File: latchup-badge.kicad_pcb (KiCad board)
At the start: 2 copper layers, 85.7 x 54 mm, 47 parts, among them J1 USB_C_Receptacle_USB2.0, J2 Connector_Generic:Conn_02x06_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, J3 Connector_Generic:Conn_02x06_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, J4 Connector_Generic:Conn_02x05_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, SW1 SW_Push, SW2 SW_Push, U1 ICE40UP5K-SG48ITR, U2 TLV70012_SOT23-5, U3 TLV70033_SOT23-5, U4 M25PX32-VMW, U5 LY68L6400, X1 ASE-12.000MHz

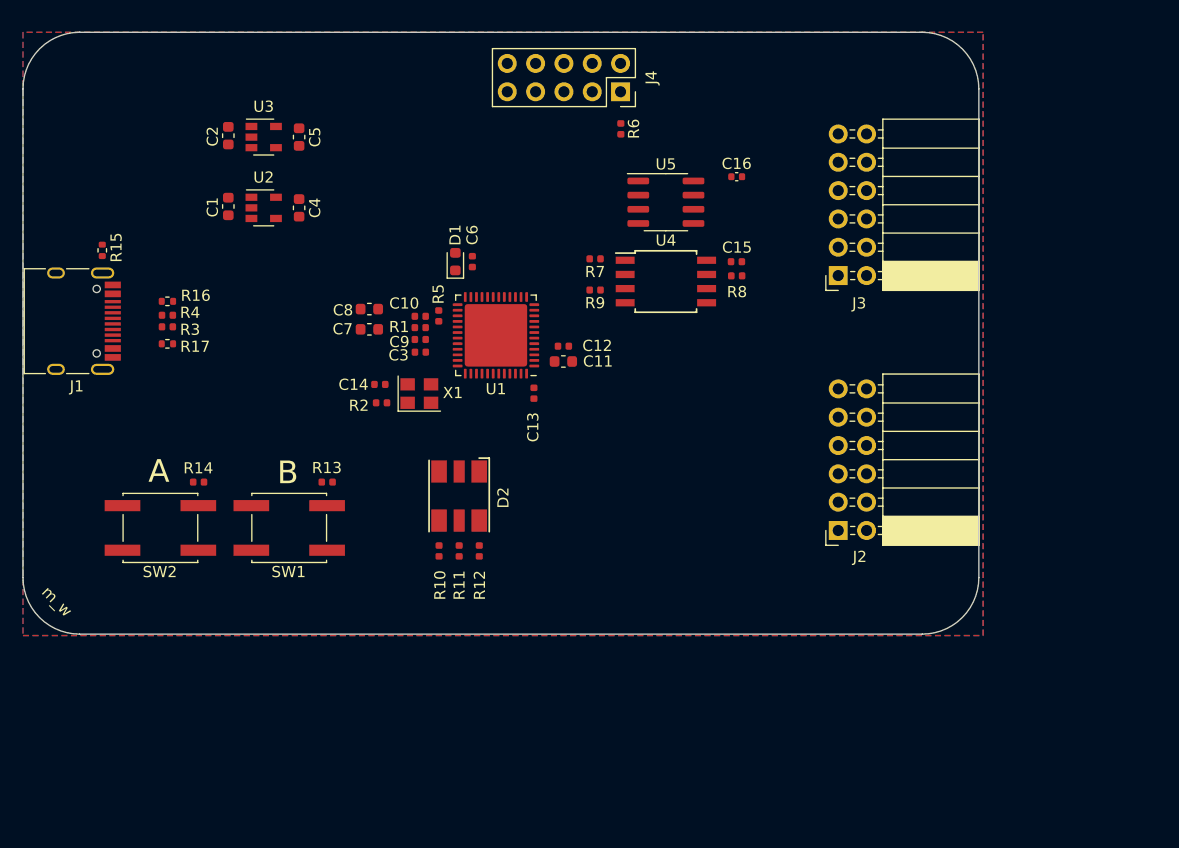
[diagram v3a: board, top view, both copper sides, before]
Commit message: Use the PMOD pinout from icebreaker bitsy breakout
Signed-off-by: Michael Welling <mwelling@ieee.org>
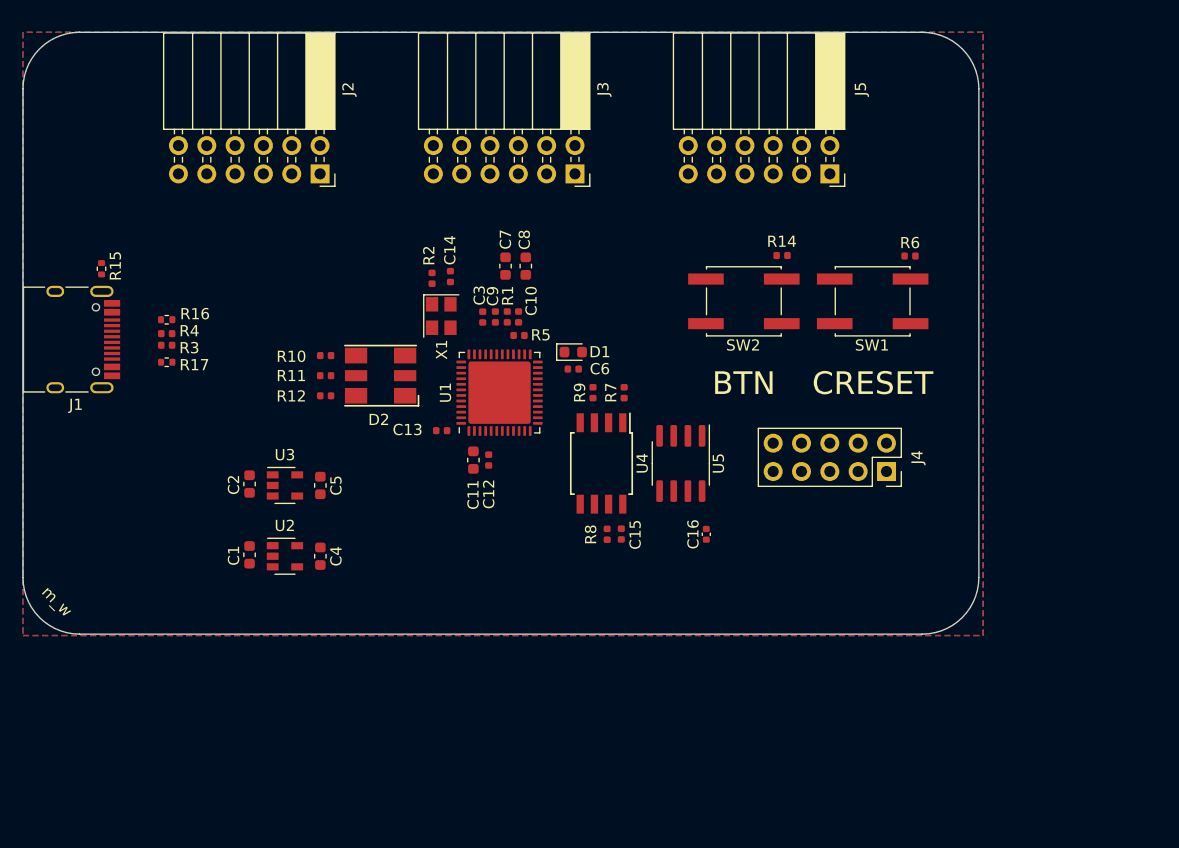
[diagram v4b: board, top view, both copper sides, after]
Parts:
- removed R13: 10K, Resistor_SMD:R_0402_1005Metric
- added J5: Connector_Generic:Conn_02x06_Odd_Even, Connector_PinSocket_2.54mm:PinSocket_2x06_P2.54mm_Horizontal, F.Cu at (148.6, 63.5)
- moved J2 56.4 mm to (102.8, 63.5), turned to -90 degrees
- moved SW1 56.1 mm to (152.4, 74.9)
- moved R14 56.1 mm to (144.3, 70.8)
- moved SW2 56.1 mm to (140.8, 74.9)
- moved J4 41.6 mm to (153.6, 90.2)
- moved C16 32.2 mm to (137.5, 95.8), turned to 90 degrees
- moved C2 31.3 mm to (96.5, 91.3)
- moved C4 31.3 mm to (102.9, 97.8)
- moved U2 31.3 mm to (99.7, 97.8)
- moved C5 31.3 mm to (102.9, 91.4)
- moved U3 31.3 mm to (99.7, 91.4)
- moved C1 31.3 mm to (96.5, 97.7)
- moved R6 28.3 mm to (155.8, 70.9), turned to 0 degrees
- moved C15 26.5 mm to (129.9, 95.8), turned to 90 degrees
- moved R8 25.9 mm to (128.6, 95.8), turned to -90 degrees
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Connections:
- net Net-(U1-Pad35) renamed /PIN35
- J2 pad 1: /J2_P1 -> +3V3
- J2 pad 10: +3V3 -> /PIN45
- J2 pad 11: GND -> /PIN47
- J2 pad 12: GND -> /PIN44
- J2 pad 2: /J2_P2 -> +3V3
- J2 pad 3: /J2_P3 -> GND
- J2 pad 4: /J2_P4 -> GND
- J2 pad 5: /J2_P5 -> /PIN9
- J2 pad 6: /J2_P6 -> /PIN10
- J2 pad 7: /J2_P7 -> /PIN4
- J2 pad 8: /J2_P8 -> /PIN3
- J2 pad 9: +3V3 -> /PIN48
- J3 pad 1: /J3_P1 -> +3V3
- J3 pad 10: +3V3 -> /PIN31
- J3 pad 11: GND -> /PIN43
- J3 pad 12: GND -> /PIN36
- J3 pad 2: /J3_P2 -> +3V3
- J3 pad 3: /J3_P3 -> GND
- J3 pad 4: /J3_P4 -> GND
- J3 pad 5: /J3_P5 -> /PIN28
- J3 pad 6: /J3_P6 -> /PIN34
- J3 pad 7: /J3_P7 -> /PIN26
- J3 pad 8: /J3_P8 -> /PIN27
- J3 pad 9: +3V3 -> /PIN32
- R3 pad 1: /USBD- -> /USBD_N
- R4 pad 1: /USBD+ -> /USBD_P
- R5 pad 1: Net-(R5-Pad1) -> /USB_DET
- R5 pad 2: /USBD+ -> /USBD_P
- SW1 pad 2: /BTN_B -> /CRESET
- U1 pad 10: /J3_P6 -> /PIN10
- U1 pad 11: /J3_P5 -> /PIN11
- U1 pad 12: /J3_P8 -> /PIN12
- U1 pad 13: /J3_P7 -> /PIN13
- U1 pad 18: /RX -> /FLASH_IO2_WP
- U1 pad 19: /TX -> /FLASH_IO3_HLD
- U1 pad 2: unconnected-(U1-Pad2) -> /BTN_A
- U1 pad 20: /FLASH_IO3_HLD -> /PIN20
- U1 pad 21: /FLASH_IO2_WP -> /PIN21
- U1 pad 23: /BTN_B -> /PIN23
- U1 pad 25: /BTN_A -> /PIN25
- U1 pad 26: /USBD- -> /PIN26
- U1 pad 27: /USBD+ -> /PIN27
- U1 pad 28: Net-(R5-Pad1) -> /PIN28
- U1 pad 3: /SS_PSRAM -> /PIN3
- U1 pad 31: unconnected-(U1-Pad31) -> /PIN31
- U1 pad 32: unconnected-(U1-Pad32) -> /PIN32
- U1 pad 34: unconnected-(U1-Pad34) -> /PIN34
- U1 pad 36: /J2_P2 -> /PIN36
- U1 pad 37: /J2_P1 -> /USB_DET
- U1 pad 38: /J2_P4 -> /USBD_N
- U1 pad 4: unconnected-(U1-Pad4) -> /PIN4
- U1 pad 42: /J2_P3 -> /USBD_P
- U1 pad 43: /J2_P6 -> /PIN43
- U1 pad 44: /J2_P5 -> /PIN44
- U1 pad 45: /J2_P8 -> /PIN45
- U1 pad 46: /J2_P7 -> /PIN46
- U1 pad 47: /J3_P2 -> /PIN47
- U1 pad 48: /J3_P1 -> /PIN48
- U1 pad 6: /J3_P4 -> /SS_PSRAM
- U1 pad 9: /J3_P3 -> /PIN9
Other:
- board text added: "BTN"
- board text added: "CRESET"
- board text removed: "A"
- board text removed: "B"

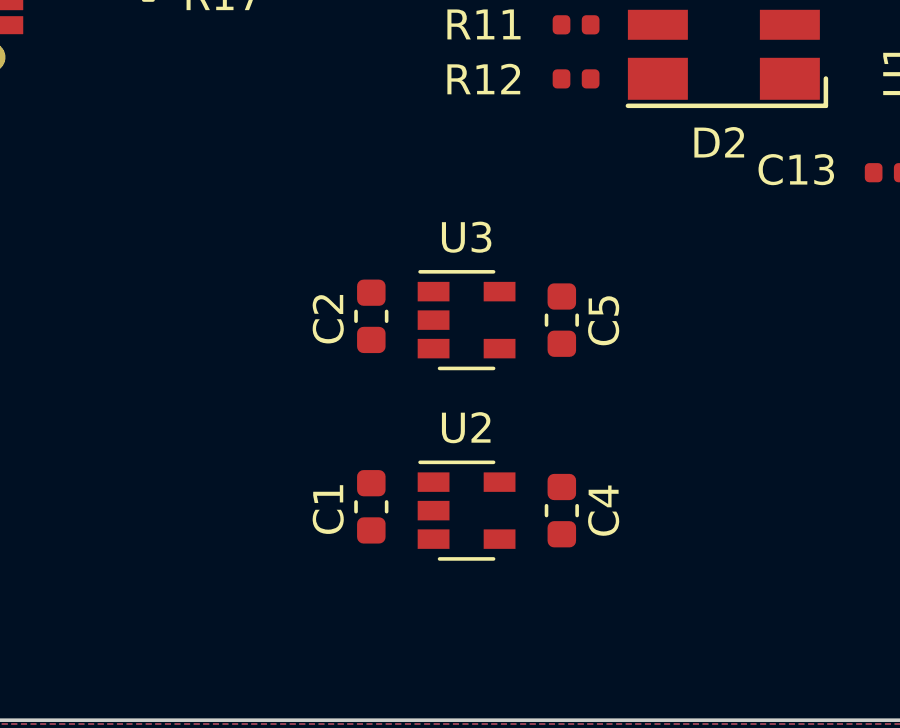
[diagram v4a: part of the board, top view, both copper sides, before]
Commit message: Add delay to 3.3V enable
The 1.2V rail should be up before 3.3V.

Signed-off-by: Michael Welling <mwelling@ieee.org>
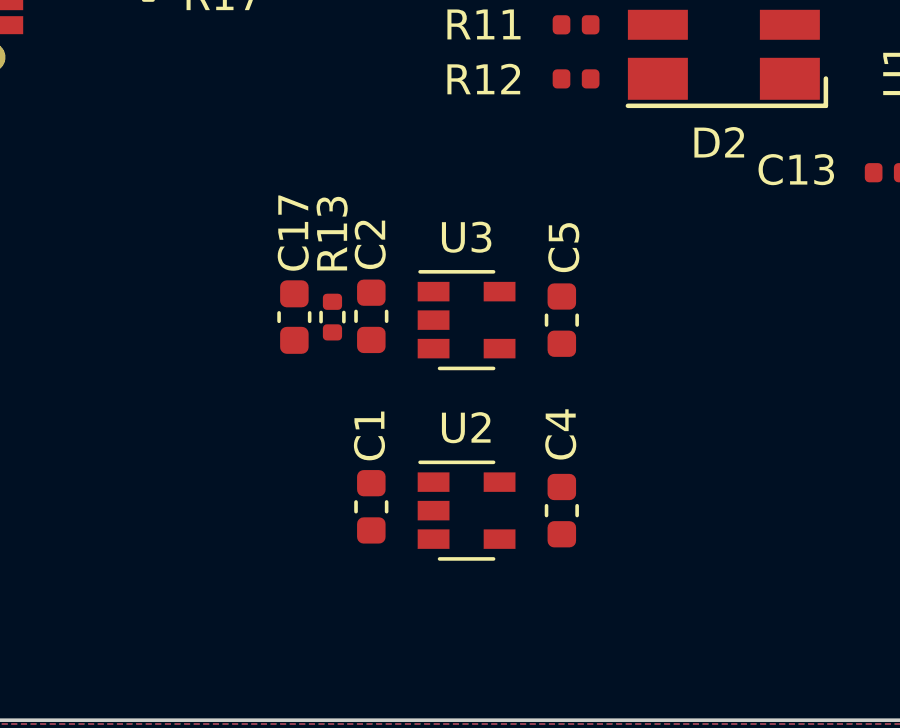
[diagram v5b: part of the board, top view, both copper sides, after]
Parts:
- added C17: 1uF, Capacitor_SMD:C_0603_1608Metric, F.Cu at (94.0, 91.3)
- added R13: 10K, Resistor_SMD:R_0402_1005Metric, F.Cu at (95.2, 91.3)
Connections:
- J4 pad 4: /TX -> unconnected-(J4-Pad4)
- J4 pad 6: /RX -> unconnected-(J4-Pad6)
- U3 pad 3: +5V -> Net-(U3-Pad3)
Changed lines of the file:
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@@
   (net 41 "/PIN25")
   (net 42 "/USBD_N")
-  (net 43 "/RX")
-  (net 44 "/TX")
+  (net 43 "Net-(U3-Pad3)")
+  (net 44 "unconnected-(J4-Pad4)")
   (net 45 "/CDONE")
   (net 46 "/CRESET")
@@
   (net 61 "/USB_DET")
   (net 62 "/PIN35")
+  (net 63 "unconnected-(J4-Pad6)")
   (footprint "Capacitor_SMD:C_0603_1608Metric" (layer "F.Cu")
     (at 96.52 97.663 -90)
@@
     (property "Sheetname" "")
     (attr smd)
-    (fp_text reference "C1" (at 0.066288 1.399799 90) (layer "F.SilkS")
+    (fp_text reference "C1" (at -2.3876 0.0254 90) (layer "F.SilkS")
       (effects (font (size 1 1) (thickness 0.15)))
     )
@@
     (property "Sheetname" "")
     (attr smd)
-    (fp_text reference "C5" (at 0 -1.43 90) (layer "F.SilkS")
+    (fp_text reference "C5" (at -2.4384 -0.1016 90) (layer "F.SilkS")
       (effects (font (size 1 1) (thickness 0.15)))
     )
@@
       (net 8 "GND") (pinfunction "GND") (pintype "power_in"))
     (pad "3" smd rect locked (at -1.1 0.95) (size 1.06 0.65) (layers "F.Cu" "F.Paste" "F.Mask")
-      (net 9 "+5V") (pinfunction "EN") (pintype "input"))
+      (net 43 "Net-(U3-Pad3)") (pinfunction "EN") (pintype "input"))
     (pad "4" smd rect locked (at 1.1 0.95) (size 1.06 0.65) (layers "F.Cu" "F.Paste" "F.Mask")
       (net 22 "unconnected-(U3-Pad4)") (pinfunction "NC") (pintype "no_connect"))
@@
     (property "Sheetname" "")
     (attr smd)
-    (fp_text reference "C4" (at 0 -1.43 90) (layer "F.SilkS")
+    (fp_text reference "C4" (at -2.54 0 90) (layer "F.SilkS")
       (effects (font (size 1 1) (thickness 0.15)))
     )
@@
     (property "Sheetname" "")
     (attr smd)
-    (fp_text reference "C2" (at 0.066288 1.399799 90) (layer "F.SilkS")
+    (fp_text reference "C2" (at -2.413 0 90) (layer "F.SilkS")
       (effects (font (size 1 1) (thickness 0.15)))
     )
@@
       (net 20 "/ICE40_SPI_SO") (pinfunction "Pin_3") (pintype "passive"))
     (pad "4" thru_hole oval locked (at -2.54 2.54 270) (size 1.7 1.7) (drill 1) (layers *.Cu *.Mask)
-      (net 44 "/TX") (pinfunction "Pin_4") (pintype "passive"))
+      (net 44 "unconnected-(J4-Pad4)") (pinfunction "Pin_4") (pintype "passive"))
     (pad "5" thru_hole oval locked (at 0 5.08 270) (size 1.7 1.7) (drill 1) (layers *.Cu *.Mask)
       (net 19 "/ICE40_SPI_SCK") (pinfunction "Pin_5") (pintype "passive"))
     (pad "6" thru_hole oval locked (at -2.54 5.08 270) (size 1.7 1.7) (drill 1) (layers *.Cu *.Mask)
-      (net 43 "/RX") (pinfunction "Pin_6") (pintype "passive"))
+      (net 63 "unconnected-(J4-Pad6)") (pinfunction "Pin_6") (pintype "passive"))
     (pad "7" thru_hole oval locked (at 0 7.62 270) (size 1.7 1.7) (drill 1) (layers *.Cu *.Mask)
       (net 18 "/ICE40_SPI_SS") (pinfunction "Pin_7") (pintype "passive"))
@@
       (net 10 "+3V3") (pintype "passive"))
     (model "${KISYS3DMOD}/Resistor_SMD.3dshapes/R_0402_1005Metric.wrl"
+      (offset (xyz 0 0 0))
+      (scale (xyz 1 1 1))
+      (rotate (xyz 0 0 0))
+    )
+  )
+  (footprint "Capacitor_SMD:C_0603_1608Metric" (layer "F.Cu")
+    (at 93.9546 91.3384 90)
+    (descr "Capacitor SMD 0603 (1608 Metric), square (rectangular) end terminal, IPC_7351 nominal, (Body size source: IPC-SM-782 page 76, https://www.pcb-3d.com/wordpress/wp-content/uploads/ipc-sm-782a_amendment_1_and_2.pdf), generated with kicad-footprint-generator")
+    (tags "capacitor")
+    (property "Sheetfile" "latchup-badge.kicad_sch")
+    (property "Sheetname" "")
+    (attr smd)
+    (fp_text reference "C17" (at 2.8194 0 90) (layer "F.SilkS")
+      (effects (font (size 1 1) (thickness 0.15)))
+    )
+    (fp_text value "1uF" (at 0 1.43 90) (layer "F.Fab")
+      (effects (font (size 1 1) (thickness 0.15)))
+    )
+    (fp_text user "${REFERENCE}" (at 0 0 90) (layer "F.Fab")
+      (effects (font (size 0.4 0.4) (thickness 0.06)))
+    )
+    (fp_line (start -0.14058 0.51) (end 0.14058 0.51) (layer "F.SilkS") (width 0.12))
+    (fp_line (start -0.14058 -0.51) (end 0.14058 -0.51) (layer "F.SilkS") (width 0.12))
+    (fp_line (start 1.48 0.73) (end -1.48 0.73) (layer "F.CrtYd") (width 0.05))
+    (fp_line (start -1.48 0.73) (end -1.48 -0.73) (layer "F.CrtYd") (width 0.05))
+    (fp_line (start 1.48 -0.73) (end 1.48 0.73) (layer "F.CrtYd") (width 0.05))
+    (fp_line (start -1.48 -0.73) (end 1.48 -0.73) (layer "F.CrtYd") (width 0.05))
+    (fp_line (start -0.8 -0.4) (end 0.8 -0.4) (layer "F.Fab") (width 0.1))
+    (fp_line (start 0.8 0.4) (end -0.8 0.4) (layer "F.Fab") (width 0.1))
+    (fp_line (start -0.8 0.4) (end -0.8 -0.4) (layer "F.Fab") (width 0.1))
+    (fp_line (start 0.8 -0.4) (end 0.8 0.4) (layer "F.Fab") (width 0.1))
+    (pad "1" smd roundrect (at -0.775 0 90) (size 0.9 0.95) (layers "F.Cu" "F.Paste" "F.Mask") (roundrect_rratio 0.25)
+      (net 43 "Net-(U3-Pad3)") (pintype "passive"))
+    (pad "2" smd roundrect (at 0.775 0 90) (size 0.9 0.95) (layers "F.Cu" "F.Paste" "F.Mask") (roundrect_rratio 0.25)
+      (net 8 "GND") (pintype "passive"))
+    (model "${KICAD6_3DMODEL_DIR}/Capacitor_SMD.3dshapes/C_0603_1608Metric.wrl"
       (offset (xyz 0 0 0))
       (scale (xyz 1 1 1))
@@
     (model "${KICAD6_3DMODEL_DIR}/Resistor_SMD.3dshapes/R_0402_1005Metric.wrl"
       (offset (xyz 0 0 0))
+      (scale (xyz 1 1 1))
+      (rotate (xyz 0 0 0))
+    )
+  )
+  (footprint "Resistor_SMD:R_0402_1005Metric" (layer "F.Cu")
+    (at 95.2246 91.3384 90)
+    (descr "Resistor SMD 0402 (1005 Metric), square (rectangular) end terminal, IPC_7351 nominal, (Body size source: IPC-SM-782 page 72, https://www.pcb-3d.com/wordpress/wp-content/uploads/ipc-sm-782a_amendment_1_and_2.pdf), generated with kicad-footprint-generator")
+    (tags "resistor")
+    (property "Sheetfile" "latchup-badge.kicad_sch")
+    (property "Sheetname" "")
+    (attr smd)
+    (fp_text reference "R13" (at 2.7686 0.0254 90) (layer "F.SilkS")
+      (effects (font (size 1 1) (thickness 0.15)))
+    )
+    (fp_text value "10K" (at 0 1.17 90) (layer "F.Fab")
+      (effects (font (size 1 1) (thickness 0.15)))
+    )
+    (fp_text user "${REFERENCE}" (at 0 0 90) (layer "F.Fab")
+      (effects (font (size 0.26 0.26) (thickness 0.04)))
+    )
+    (fp_line (start -0.153641 -0.38) (end 0.153641 -0.38) (layer "F.SilkS") (width 0.12))
+    (fp_line (start -0.153641 0.38) (end 0.153641 0.38) (layer "F.SilkS") (width 0.12))
+    (fp_line (start -0.93 0.47) (end -0.93 -0.47) (layer "F.CrtYd") (width 0.05))
+    (fp_line (start 0.93 -0.47) (end 0.93 0.47) (layer "F.CrtYd") (width 0.05))
+    (fp_line (start 0.93 0.47) (end -0.93 0.47) (layer "F.CrtYd") (width 0.05))
+    (fp_line (start -0.93 -0.47) (end 0.93 -0.47) (layer "F.CrtYd") (width 0.05))
+    (fp_line (start 0.525 0.27) (end -0.525 0.27) (layer "F.Fab") (width 0.1))
+    (fp_line (start -0.525 -0.27) (end 0.525 -0.27) (layer "F.Fab") (width 0.1))
+    (fp_line (start -0.525 0.27) (end -0.525 -0.27) (layer "F.Fab") (width 0.1))
+    (fp_line (start 0.525 -0.27) (end 0.525 0.27) (layer "F.Fab") (width 0.1))
+    (pad "1" smd roundrect (at -0.51 0 90) (size 0.54 0.64) (layers "F.Cu" "F.Paste" "F.Mask") (roundrect_rratio 0.25)
+      (net 43 "Net-(U3-Pad3)") (pintype "passive"))
+    (pad "2" smd roundrect (at 0.51 0 90) (size 0.54 0.64) (layers "F.Cu" "F.Paste" "F.Mask") (roundrect_rratio 0.25)
+      (net 9 "+5V") (pintype "passive"))
+    (model "${KICAD6_3DMODEL_DIR}/Resistor_SMD.3dshapes/R_0402_1005Metric.wrl"
+      (offset (xyz 0 0 0))

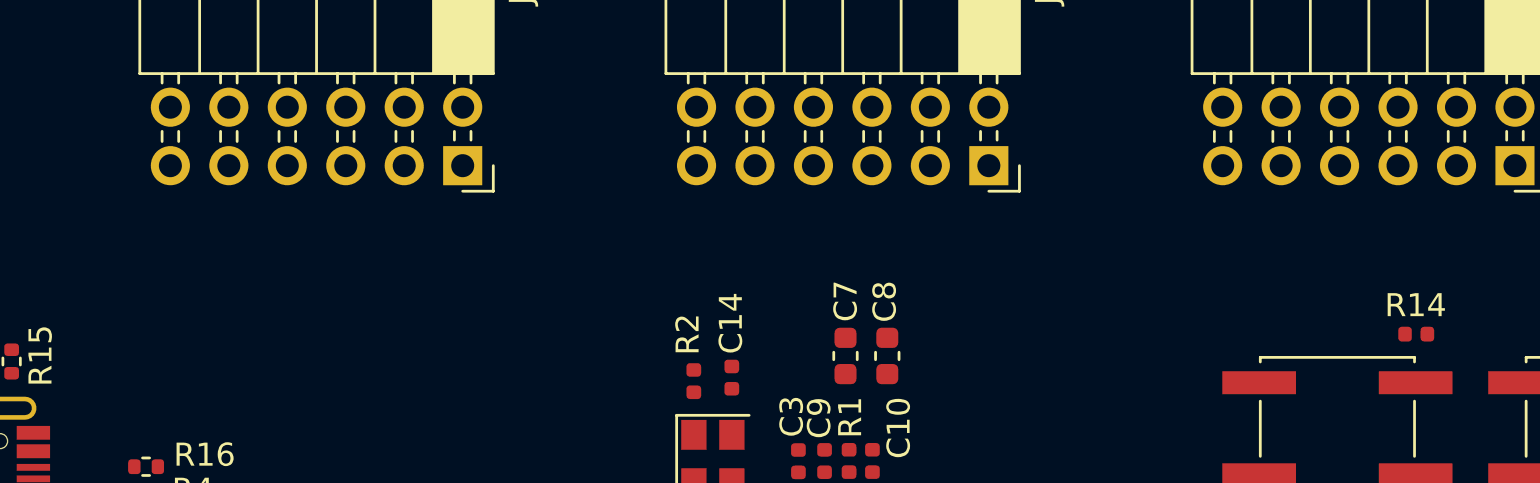
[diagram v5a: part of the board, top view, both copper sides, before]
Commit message: Add series damping resistors on PMODs
Signed-off-by: Michael Welling <mwelling@ieee.org>
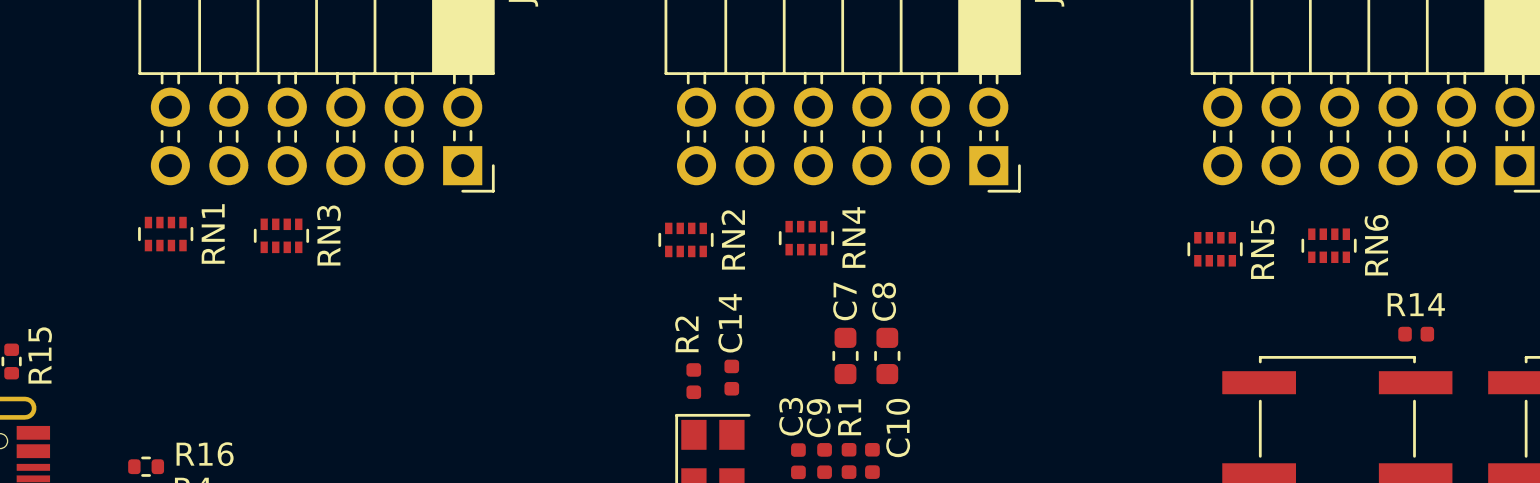
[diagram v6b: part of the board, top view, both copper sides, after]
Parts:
- added RN1: 33, Resistor_SMD:R_Array_Concave_4x0402, F.Cu at (89.9, 66.5)
- added RN2: 33, Resistor_SMD:R_Array_Concave_4x0402, F.Cu at (112.5, 66.7)
- added RN3: 33, Resistor_SMD:R_Array_Concave_4x0402, F.Cu at (95.0, 66.5)
- added RN4: 33, Resistor_SMD:R_Array_Concave_4x0402, F.Cu at (117.8, 66.6)
- added RN5: 33, Resistor_SMD:R_Array_Concave_4x0402, F.Cu at (135.5, 67.1)
- added RN6: 33, Resistor_SMD:R_Array_Concave_4x0402, F.Cu at (140.5, 67.0)
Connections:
- J2 pad 10: /PIN45 -> /P45
- J2 pad 11: /PIN47 -> /P47
- J2 pad 12: /PIN44 -> /P44
- J2 pad 5: /PIN9 -> /P9
- J2 pad 6: /PIN10 -> /P10
- J2 pad 7: /PIN4 -> /P4
- J2 pad 8: /PIN3 -> /P3
- J2 pad 9: /PIN48 -> /P48
- J3 pad 10: /PIN31 -> /P31
- J3 pad 11: /PIN43 -> /P43
- J3 pad 12: /PIN36 -> /P36
- J3 pad 5: /PIN28 -> /P28
- J3 pad 6: /PIN34 -> /P34
- J3 pad 7: /PIN26 -> /P26
- J3 pad 8: /PIN27 -> /P27
- J3 pad 9: /PIN32 -> /P32
- J5 pad 10: /PIN21 -> /P21
- J5 pad 11: /PIN23 -> /P23
- J5 pad 12: /PIN25 -> /P25
- J5 pad 5: /PIN11 -> /P11
- J5 pad 6: /PIN46 -> /P46
- J5 pad 7: /PIN13 -> /P13
- J5 pad 8: /PIN20 -> /P20
- J5 pad 9: /PIN12 -> /P12
